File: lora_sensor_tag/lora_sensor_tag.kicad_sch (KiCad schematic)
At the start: 0 parts

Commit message: lora_tag_sensor: Add shematic design
The shematic design for the following components has been added:
- MCU main part (ESP32 part)
- Power supply (completed)

Signed-off-by: Volodymyr <volodymyrnoha99@gmail.com>
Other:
- added sheet MCU_main_part (mcu_main_part.kicad_sch)
- added sheet power (power.kicad_sch)
- added sheet usb_and_prog (usb_and_prog.kicad_sch)
- note added: "LoRa Sensor TAG main sheet"

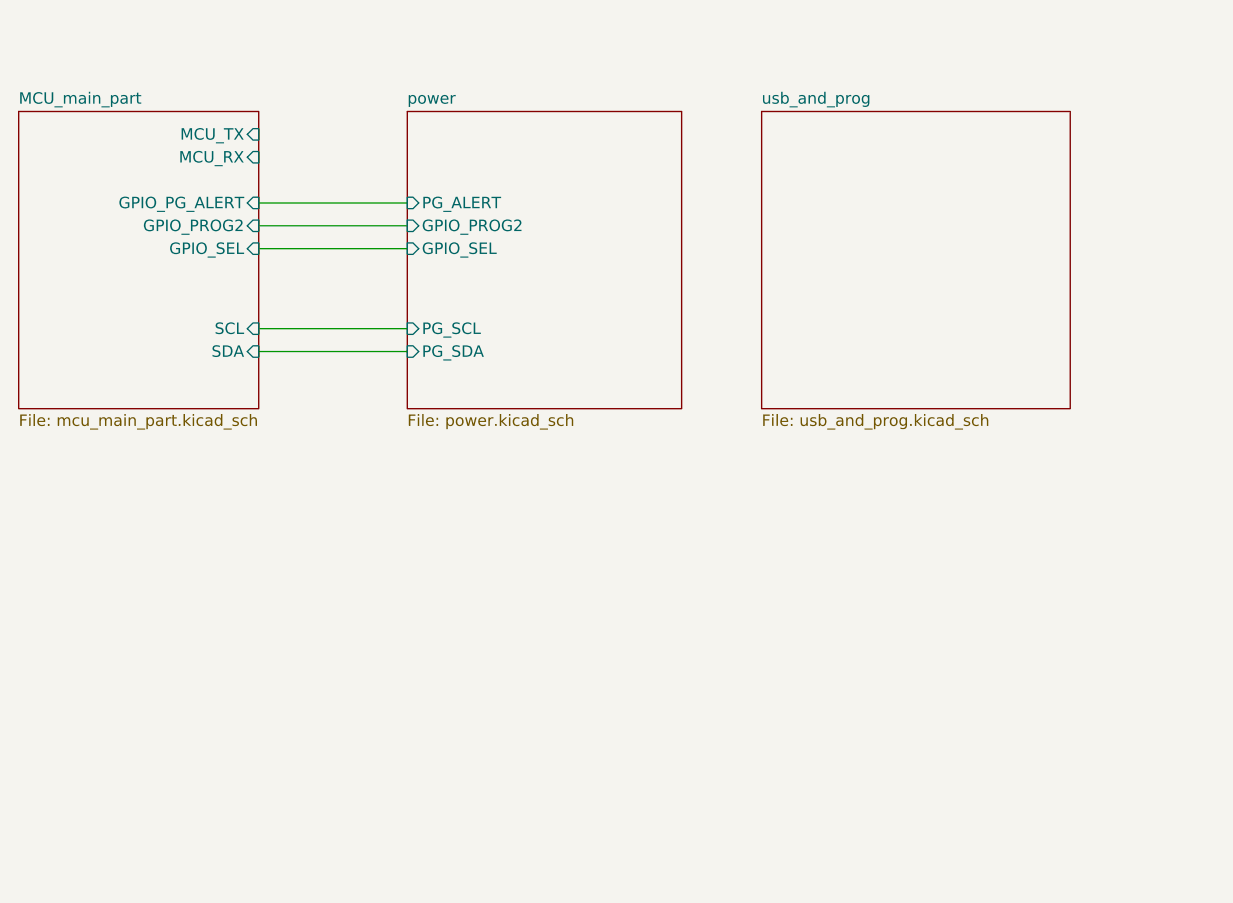
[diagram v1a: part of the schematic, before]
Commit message: lora_sensor_tag: Update shematic
Update schematic with the following changes:
 - Add SX1276 LoRa modem schematic;
 - Add antenna matching network for SX1276 LoRa modem;
 - Add PE4259 RF switch for SX1276 LoRa modem;
 - Add USB-C connector;
 - Add CP2102 USB-to-UART bridge and programming interface;

Signed-off-by: Volodymyr <volodymyrnoha99@gmail.com>
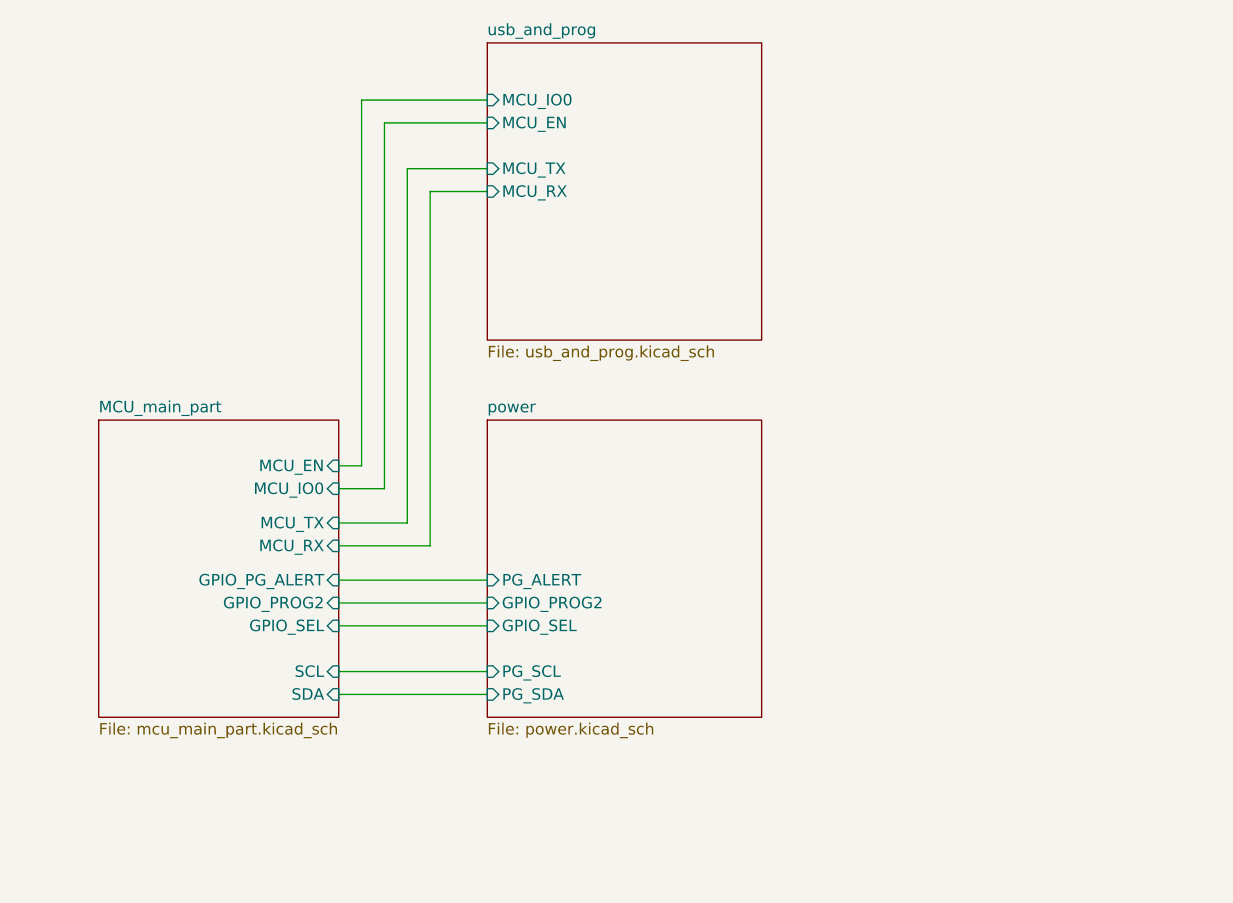
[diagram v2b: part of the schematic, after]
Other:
- sheet MCU_main_part ports: added MCU_EN, MCU_IO0; removed none
- sheet usb_and_prog ports: added MCU_EN, MCU_IO0, MCU_RX, MCU_TX; removed none
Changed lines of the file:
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@@
 	(wire
 		(pts
-			(xy 50.8 60.96) (xy 67.31 60.96)
-		)
-		(stroke
-			(width 0)
-			(type default)
-		)
-	)
-	(wire
-		(pts
-			(xy 50.8 74.93) (xy 67.31 74.93)
-		)
-		(stroke
-			(width 0)
-			(type default)
-		)
-	)
-	(wire
-		(pts
-			(xy 50.8 63.5) (xy 67.31 63.5)
-		)
-		(stroke
-			(width 0)
-			(type default)
-		)
-	)
-	(wire
-		(pts
-			(xy 50.8 77.47) (xy 67.31 77.47)
-		)
-		(stroke
-			(width 0)
-			(type default)
-		)
-	)
-	(wire
-		(pts
-			(xy 50.8 66.04) (xy 67.31 66.04)
+			(xy 76.2 52.07) (xy 64.77 52.07)
+		)
+		(stroke
+			(width 0)
+			(type default)
+		)
+	)
+	(wire
+		(pts
+			(xy 64.77 52.07) (xy 64.77 92.71)
+		)
+		(stroke
+			(width 0)
+			(type default)
+		)
+	)
+	(wire
+		(pts
+			(xy 67.31 57.15) (xy 76.2 57.15)
+		)
+		(stroke
+			(width 0)
+			(type default)
+		)
+	)
+	(wire
+		(pts
+			(xy 67.31 96.52) (xy 67.31 57.15)
+		)
+		(stroke
+			(width 0)
+			(type default)
+		)
+	)
+	(wire
+		(pts
+			(xy 69.85 59.69) (xy 76.2 59.69)
+		)
+		(stroke
+			(width 0)
+			(type default)
+		)
+	)
+	(wire
+		(pts
+			(xy 59.69 102.87) (xy 76.2 102.87)
+		)
+		(stroke
+			(width 0)
+			(type default)
+		)
+	)
+	(wire
+		(pts
+			(xy 59.69 113.03) (xy 76.2 113.03)
+		)
+		(stroke
+			(width 0)
+			(type default)
+		)
+	)
+	(wire
+		(pts
+			(xy 59.69 99.06) (xy 69.85 99.06)
+		)
+		(stroke
+			(width 0)
+			(type default)
+		)
+	)
+	(wire
+		(pts
+			(xy 64.77 92.71) (xy 59.69 92.71)
+		)
+		(stroke
+			(width 0)
+			(type default)
+		)
+	)
+	(wire
+		(pts
+			(xy 69.85 99.06) (xy 69.85 59.69)
+		)
+		(stroke
+			(width 0)
+			(type default)
+		)
+	)
+	(wire
+		(pts
+			(xy 62.23 49.53) (xy 62.23 90.17)
+		)
+		(stroke
+			(width 0)
+			(type default)
+		)
+	)
+	(wire
+		(pts
+			(xy 76.2 49.53) (xy 62.23 49.53)
+		)
+		(stroke
+			(width 0)
+			(type default)
+		)
+	)
+	(wire
+		(pts
+			(xy 59.69 105.41) (xy 76.2 105.41)
+		)
+		(stroke
+			(width 0)
+			(type default)
+		)
+	)
+	(wire
+		(pts
+			(xy 59.69 96.52) (xy 67.31 96.52)
+		)
+		(stroke
+			(width 0)
+			(type default)
+		)
+	)
+	(wire
+		(pts
+			(xy 59.69 115.57) (xy 76.2 115.57)
+		)
+		(stroke
+			(width 0)
+			(type default)
+		)
+	)
+	(wire
+		(pts
+			(xy 59.69 107.95) (xy 76.2 107.95)
+		)
+		(stroke
+			(width 0)
+			(type default)
+		)
+	)
+	(wire
+		(pts
+			(xy 62.23 90.17) (xy 59.69 90.17)
 		)
 		(stroke
@@
 	)
 	(sheet
-		(at 24.13 50.8)
+		(at 33.02 85.09)
 		(size 26.67 33.02)
 		(exclude_from_sim no)
@@
 		)
 		(property "Sheetname" "MCU_main_part"
-			(at 24.13 50.0884 0)
+			(at 33.02 84.3784 0)
 			(show_name no)
 			(do_not_autoplace no)
@@
 		)
 		(property "Sheetfile" "mcu_main_part.kicad_sch"
-			(at 24.13 84.4046 0)
+			(at 33.02 118.6946 0)
 			(show_name no)
 			(do_not_autoplace no)
@@
 		)
 		(pin "GPIO_PG_ALERT" input
-			(at 50.8 60.96 0)
+			(at 59.69 102.87 0)
 			(effects
 				(font
@@
 		)
 		(pin "GPIO_PROG2" input
-			(at 50.8 63.5 0)
+			(at 59.69 105.41 0)
 			(effects
 				(font
@@
 		)
 		(pin "GPIO_SEL" input
-			(at 50.8 66.04 0)
+			(at 59.69 107.95 0)
 			(effects
 				(font
@@
 		)
 		(pin "MCU_RX" input
-			(at 50.8 55.88 0)
+			(at 59.69 99.06 0)
 			(effects
 				(font
@@
 		)
 		(pin "MCU_TX" input
-			(at 50.8 53.34 0)
+			(at 59.69 96.52 0)
 			(effects
 				(font
@@
 		)
 		(pin "SCL" input
-			(at 50.8 74.93 0)
+			(at 59.69 113.03 0)
 			(effects
 				(font
@@
 		)
 		(pin "SDA" input
-			(at 50.8 77.47 0)
+			(at 59.69 115.57 0)
+			(effects
+				(font
+					(size 1.27 1.27)
+				)
+				(justify right)
+			)
+		)
+		(pin "MCU_EN" input
+			(at 59.69 90.17 0)
+			(effects
+				(font
+					(size 1.27 1.27)
+				)
+				(justify right)
+			)
+		)
+		(pin "MCU_IO0" input
+			(at 59.69 92.71 0)
 			(effects
 				(font
@@
 	)
 	(sheet
-		(at 67.31 50.8)
+		(at 76.2 85.09)
 		(size 30.48 33.02)
 		(exclude_from_sim no)
@@
 		)
 		(property "Sheetname" "power"
-			(at 67.31 50.0884 0)
+			(at 76.2 84.3784 0)
 			(show_name no)
 			(do_not_autoplace no)
@@
 		)
 		(property "Sheetfile" "power.kicad_sch"
-			(at 67.31 84.4046 0)
+			(at 76.2 118.6946 0)
 			(show_name no)
 			(do_not_autoplace no)
@@
 		)
 		(pin "GPIO_PROG2" input
-			(at 67.31 63.5 180)
+			(at 76.2 105.41 180)
 			(effects
 				(font
@@
 		)
 		(pin "GPIO_SEL" input
-			(at 67.31 66.04 180)
+			(at 76.2 107.95 180)
 			(effects
 				(font
@@
 		)
 		(pin "PG_ALERT" input
-			(at 67.31 60.96 180)
+			(at 76.2 102.87 180)
 			(effects
 				(font
@@
 		)
 		(pin "PG_SCL" input
-			(at 67.31 74.93 180)
+			(at 76.2 113.03 180)
 			(effects
 				(font
@@
 		)
 		(pin "PG_SDA" input
-			(at 67.31 77.47 180)
+			(at 76.2 115.57 180)
 			(effects
 				(font
@@
 	)
 	(sheet
-		(at 106.68 50.8)
-		(size 34.29 33.02)
+		(at 76.2 43.18)
+		(size 30.48 33.02)
 		(exclude_from_sim no)
 		(in_bom yes)
@@
 		)
 		(property "Sheetname" "usb_and_prog"
-			(at 106.68 50.0884 0)
+			(at 76.2 42.4684 0)
 			(show_name no)
 			(do_not_autoplace no)
@@
 		)
 		(property "Sheetfile" "usb_and_prog.kicad_sch"
-			(at 106.68 84.4046 0)
+			(at 76.2 76.7846 0)
 			(show_name no)
 			(do_not_autoplace no)
@@
 			)
 		)
+		(pin "MCU_RX" input
+			(at 76.2 59.69 180)
+			(effects
+				(font
+					(size 1.27 1.27)
+				)
+				(justify left)
+			)
+		)
+		(pin "MCU_TX" input
+			(at 76.2 57.15 180)
+			(effects
+				(font
+					(size 1.27 1.27)
+				)
+				(justify left)
+			)
+		)
+		(pin "MCU_EN" input
+			(at 76.2 52.07 180)
+			(effects
+				(font
+					(size 1.27 1.27)
+				)
+				(justify left)
+			)
+		)
+		(pin "MCU_IO0" input
+			(at 76.2 49.53 180)
+			(effects
+				(font
+					(size 1.27 1.27)
+				)
+				(justify left)
+			)
+		)

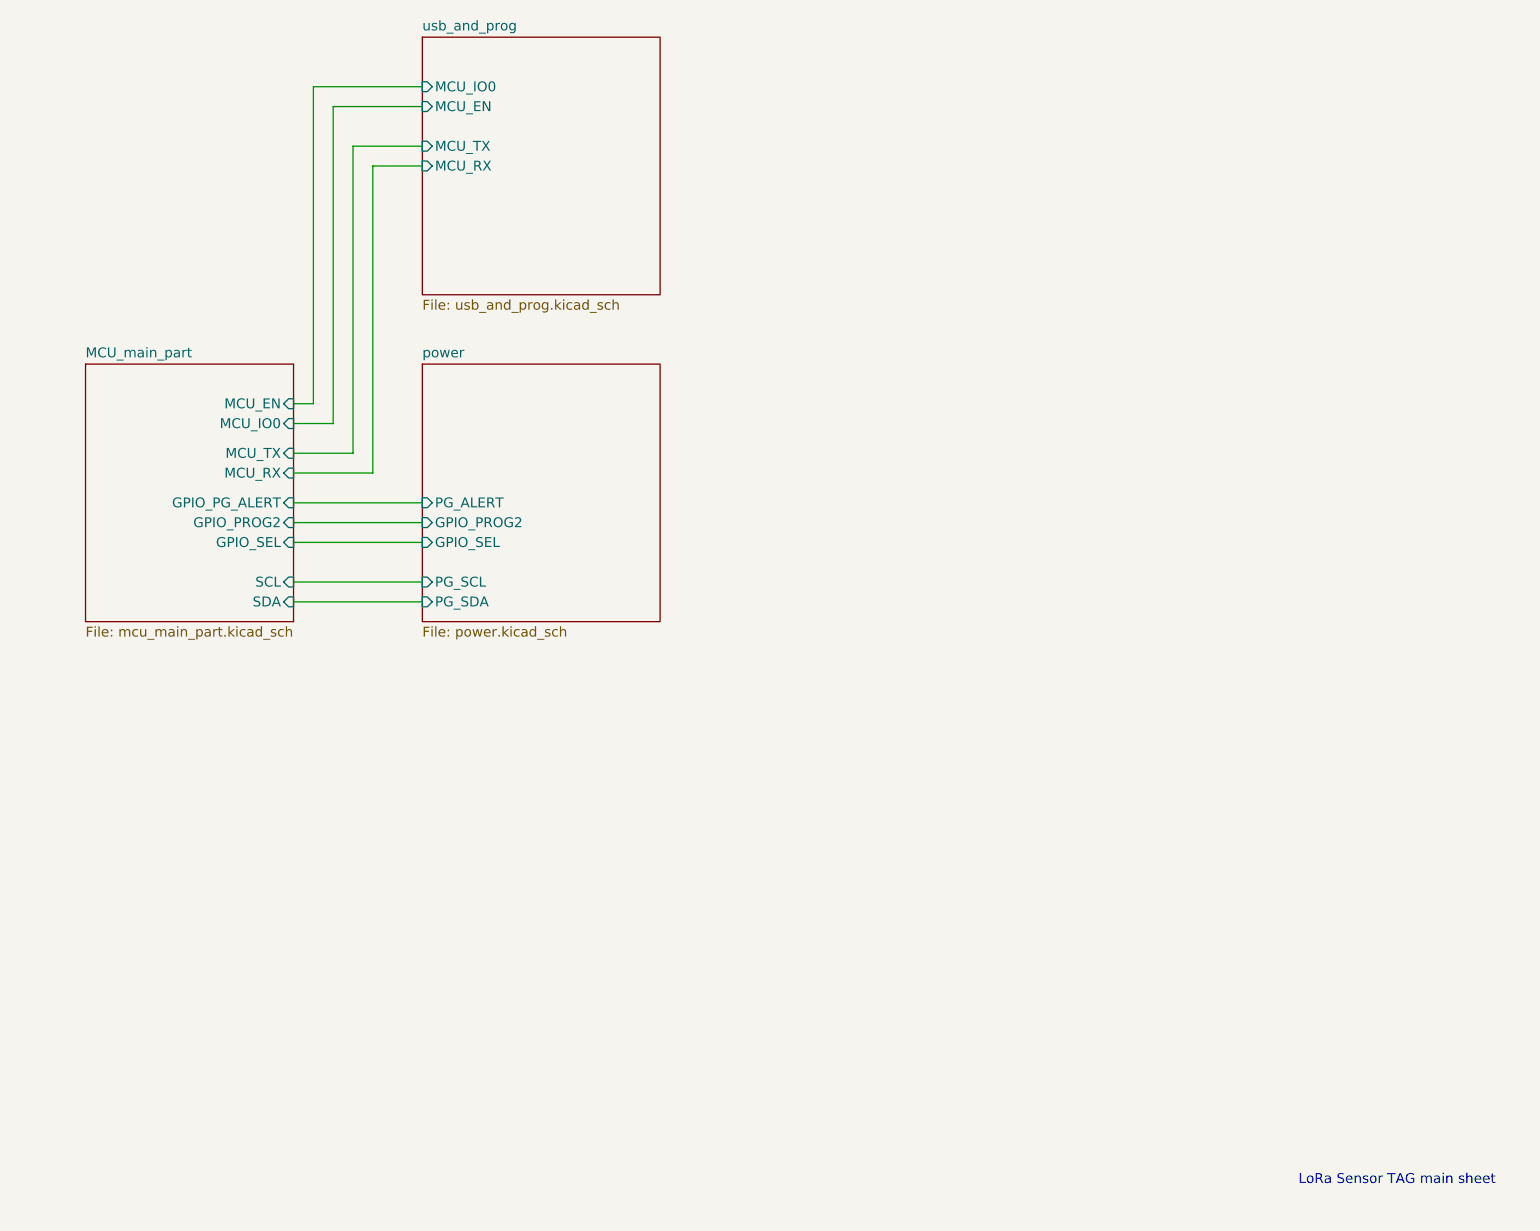
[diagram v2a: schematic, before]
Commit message: Update schematic notation and fix bugs
Global labels notation updated;
Swapped line order in schematic fixed;
Added pull-up resistor to PG-ALERT pin (fuel gauge)

Signed-off-by: Volodymyr <volodymyrnoha99@gmail.com>
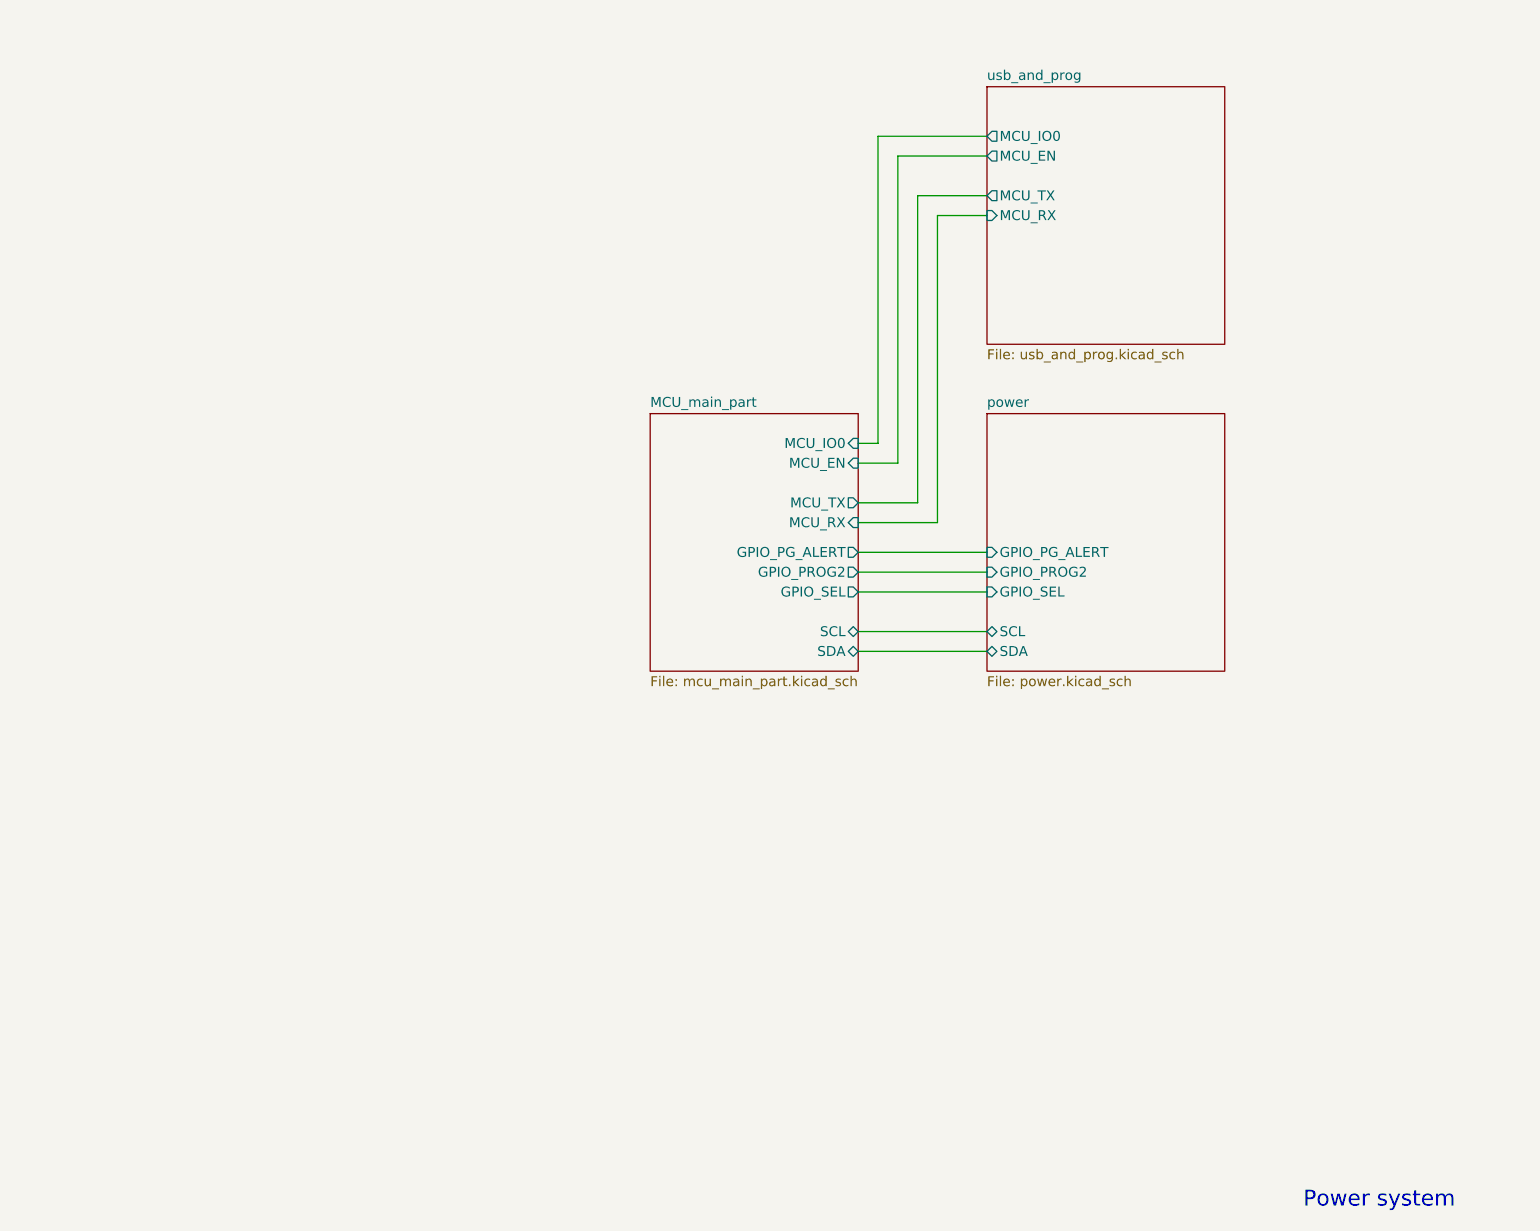
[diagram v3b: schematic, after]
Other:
- sheet power ports: added GPIO_PG_ALERT, SCL, SDA; removed PG_ALERT, PG_SCL, PG_SDA
- note added: "Power system"
- note removed: "LoRa Sensor TAG main sheet"
- title: (none) -> LoRa Sensor Tag

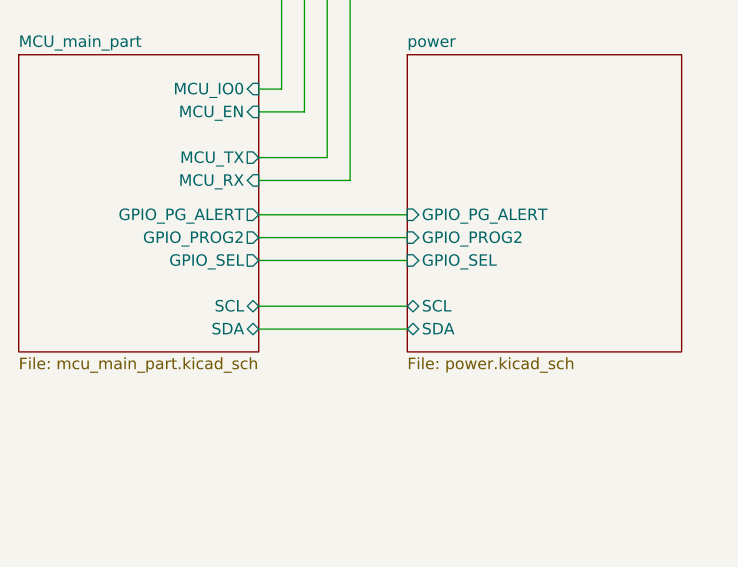
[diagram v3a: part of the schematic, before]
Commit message: Update Charge Enable mechanism on MCP73871
Adds the following charge enable control mechanism
on MCP73871:

VUSB ──|>|──┐
     D_CE1  │
            ├── V_CE_SRC ── R17 ──┬──── CE, U6.17
VBAT ──|>|──┘             47 кОм  │   |
     D_CE2                        C  R34
                                 │    |
GPIO26 ── R_B ──┬────────────── B Q3 GND
         47 кОм │                │
               R_BE              E   NPN
              100 кОм            │
                │               GND
               GND

This solution allows for controlled enabling of
the charge function  on the MCP73871, ensuring
that the charge enable pin is properly managed
through the diodes and transistor network.The
circuit allows control of the CE pin via the
GPIO26 pin and helps to keep CE in a proper state.

Signed-off-by: Volodymyr <volodymyrnoha99@gmail.com>
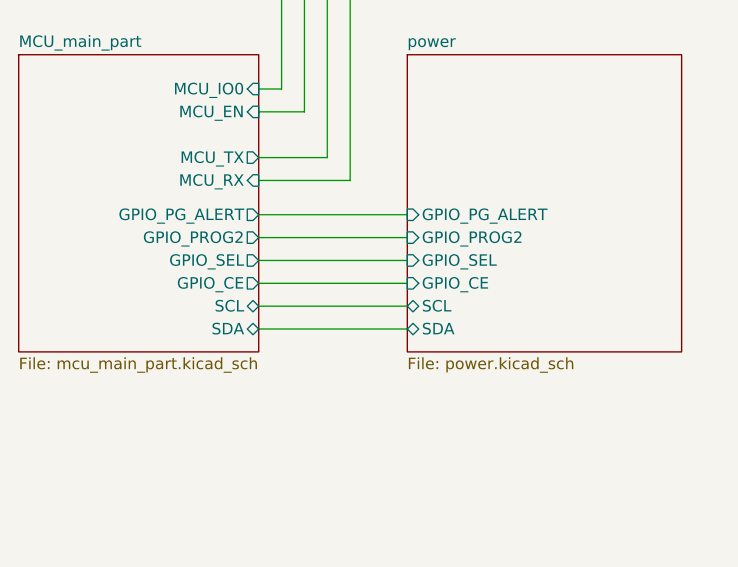
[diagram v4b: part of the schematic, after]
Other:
- sheet MCU_main_part ports: added GPIO_CE; removed none
- sheet power ports: added GPIO_CE; removed none
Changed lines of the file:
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@@
+	(wire
+		(pts
+			(xy 132.08 116.84) (xy 148.59 116.84)
+		)
+		(stroke
+			(width 0)
+			(type default)
+		)
+	)
 	(wire
 		(pts
@@
 			)
 		)
+		(pin "GPIO_CE" output
+			(at 132.08 116.84 0)
+			(effects
+				(font
+					(size 1.27 1.27)
+				)
+				(justify right)
+			)
+		)
 		(instances
 			(project "lora_sensor_tag"
@@
 			(effects
 				(font
+					(size 1.27 1.27)
+				)
+				(justify left)
+			)
+		)
+		(pin "GPIO_CE" input
+			(at 148.59 116.84 180)
+			(effects
+				(font
